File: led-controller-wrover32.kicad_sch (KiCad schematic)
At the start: 54 parts, among them J101 Molex PicoBlade 4-pin, J102 Molex PicoBlade 6-pin, J103 STATUS OUT, J104 USB_B_Micro, J105 POWER IN, J106 Molex PicoBlade 6-pin, J107 5V_LOGIC, Q101 UMH3N, U101 TPS2001DDBVX, U102 USBUF02W6, U103 ESP32-S3-WROOM-2-N32R8, U104 NTS0104BQ,115

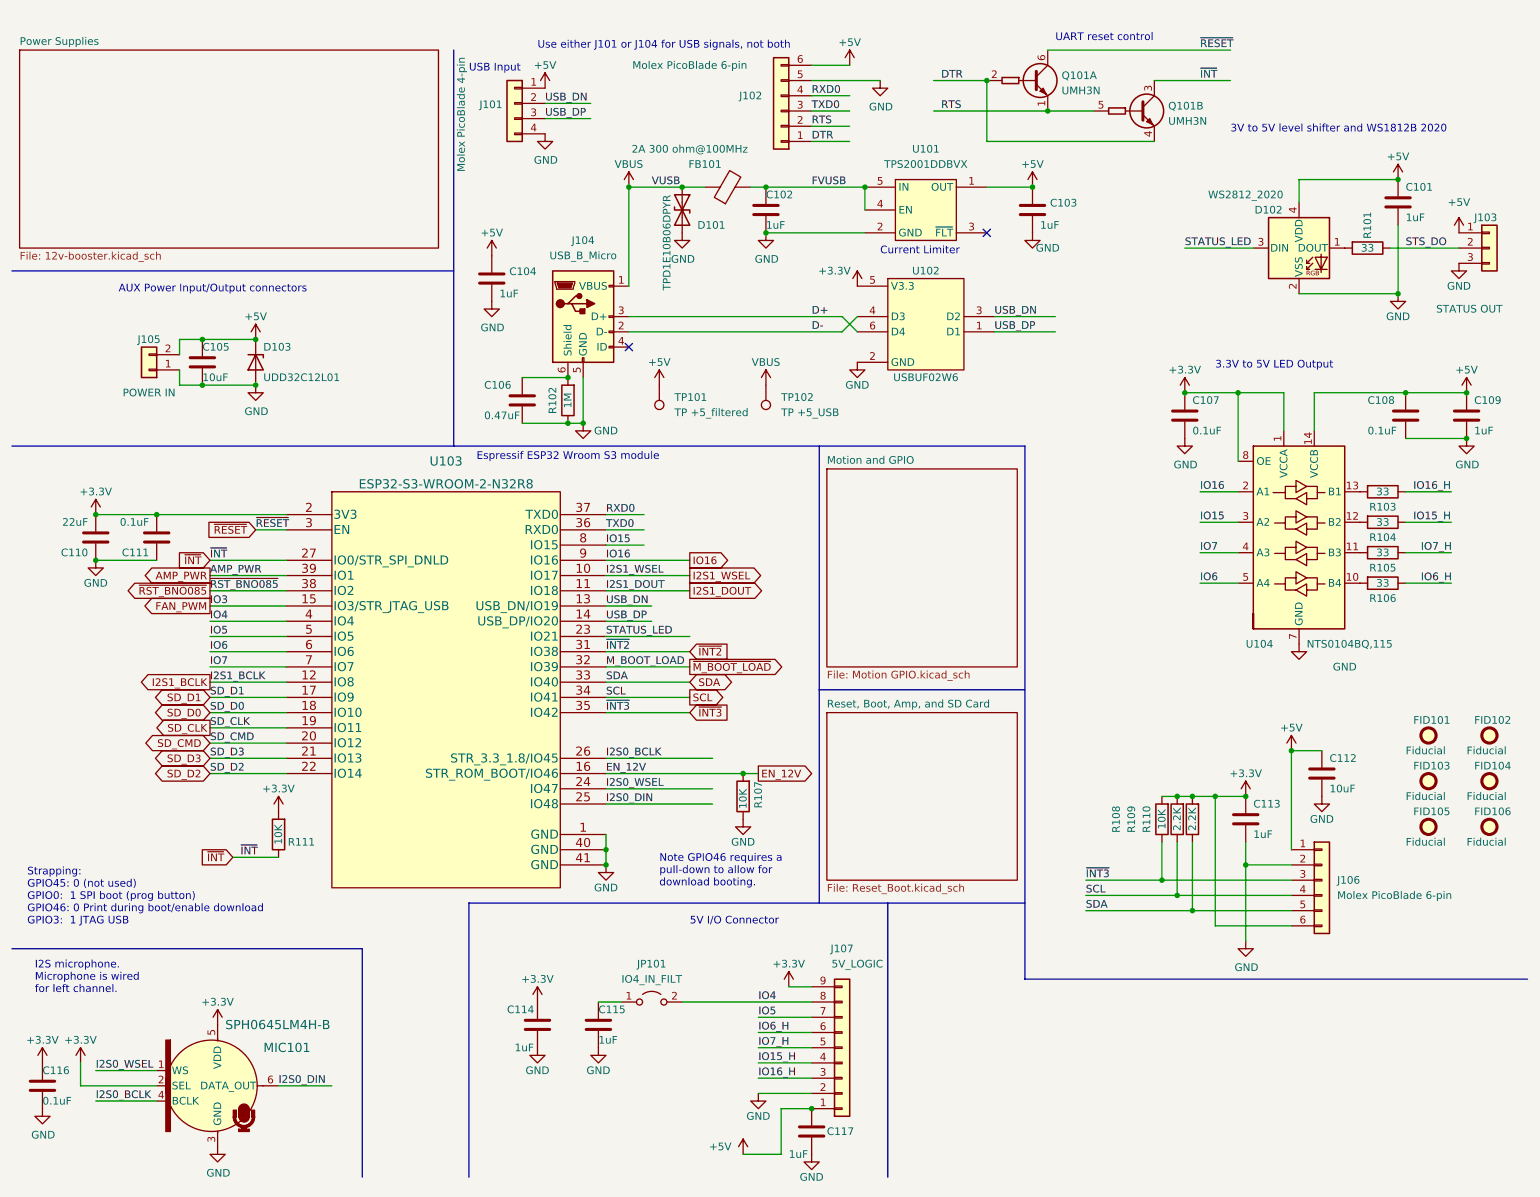
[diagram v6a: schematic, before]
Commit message: Moved to ESP32 S3 Wroom 1
The Wroom 2 requires 1.8V on a couple of GPIOs.  Since I don't need 32MB of
flash the Wroom 1 is used instead.  The footprint is slightly different,
however.

Signed-off-by: Aaron Williams <aaron.w2@gmail.com>
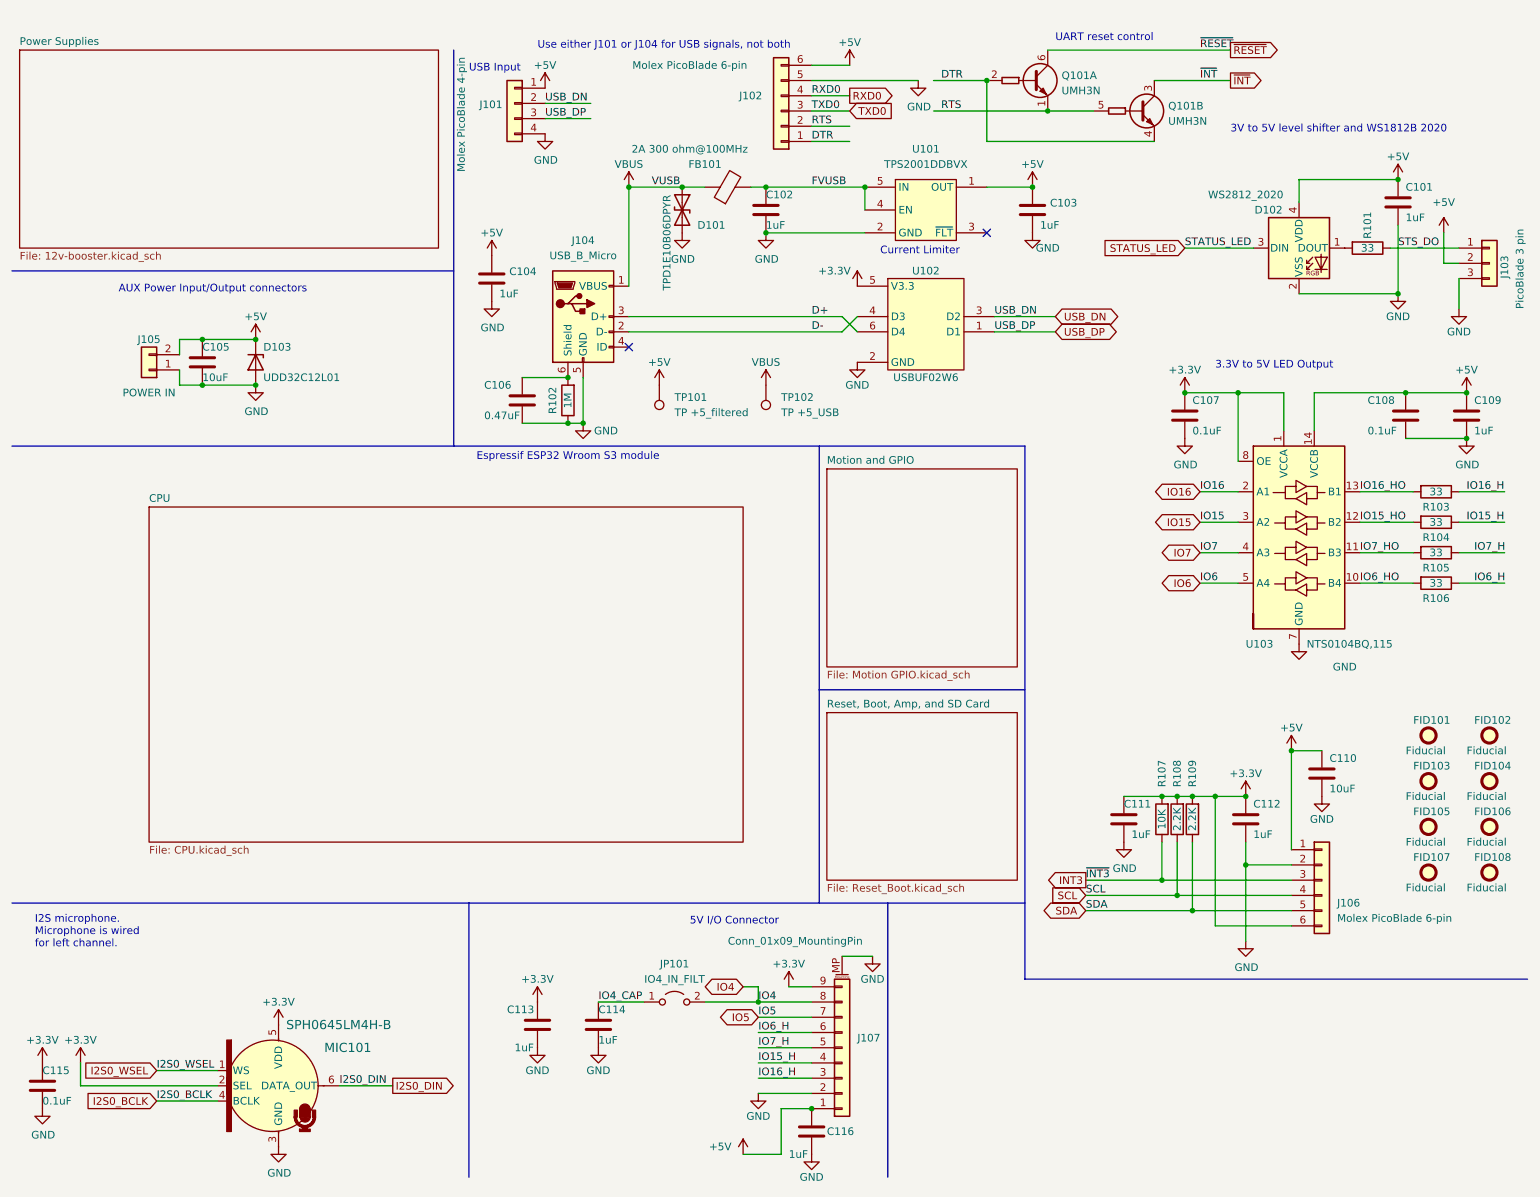
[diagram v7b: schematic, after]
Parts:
- removed C110: 22uF, Capacitor_SMD:C_0603_1608Metric, symbol Device:C
- removed J107: 5V_LOGIC, Connector_JST:JST_SH_BM09B-SRSS-TB_1x09-1MP_P1.00mm_Vertical, symbol Connector_Generic:Conn_01x09
- removed R107, R111: 10K, Resistor_SMD:R_0402_1005Metric, symbol Device:R
- removed U103: ESP32-S3-WROOM-2-N32R8, Espressif:ESP32-S3-WROOM-2, symbol Aaron:ESP32-S3-WROOM-2-N32R8V
- added FID107, FID108: Fiducial, Fiducial:Fiducial_0.5mm_Mask1mm, symbol Mechanical:Fiducial
- added J107: Conn_01x09_MountingPin, Connector_JST:JST_SH_BM09B-SRSS-TB_1x09-1MP_P1.00mm_Vertical, symbol Connector_Generic_MountingPin:Conn_01x09_MountingPin
- C111: value 0.1uF -> 1uF; DESC (none) -> CAP CER 1UF 25V X5R 0402; Digi-Key_PN (none) -> 490-GRM155R61E105MA12JCT-ND; MANUFACTURER (none) -> Murata Electronics; MFR (none) -> Murata Electronics; MPN (none) -> GRM155R61E105MA12J; Manufacturer (none) -> Murata Electronics; Manufacturer Part Number (none) -> GRM155R61E105MA12J; SPN (none) -> 490-GRM155R61E105MA12JCT-ND; SPURL (none) -> https://www.digikey.com/en/products/detail/murata-electroni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
- D103: MFR (none) -> YAGEO; MPN (none) -> UDD32C12L01; Manufacturer Part Number (none) -> UDD32C12L01; SPN (none) -> YAG6692CT-ND; SPR (none) -> Digikey; SPURL (none) -> https://www.digikey.com/en/products/detail/yageo/UDD32C12L0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
- J103: value STATUS OUT -> PicoBlade 3 pin; footprint Connector_JST:JST_SH_BM03B-SRSS-TB_1x03-1MP_P1.00mm_Vertical -> Connector_Molex:Molex_PicoBlade_53047-0310_1x03_P1.25mm_Vertical; MFR JST Sales America Inc. -> Molex; MPN BM03B-SRSS-TBT(LF)(SN) -> 0530470360; SPN 455-2957-1-ND -> 0530470360; SPURL https://www.digikey.com/en/products/detail/jst-sales-americ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 -> https://www.digikey.com/en/products/detail/molex/0530470360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
- renumbered C112 to C110, C113 to C112, C114 to C113, C115 to C114, C116 to C115, C117 to C116, R108 to R107, R109 to R108, R110 to R109, U104 to U103
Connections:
- net +3V3: now also J107.9 (Pin_9)
- net +5V: now also J103.2 (Pin_2), J107.1 (Pin_1); no longer J103.1 (Pin_1)
- net GND: now also J103.1 (Pin_1), R101.1, J107.2 (Pin_2), J107.MP (MountPin)
- net IO15_H: now also J107.4 (Pin_4)
- net IO16_H: now also J107.3 (Pin_3)
- net IO4: now also J107.8 (Pin_8)
- net IO5: now also J107.7 (Pin_7)
- net IO6_H: now also J107.6 (Pin_6)
- net IO7_H: now also J107.5 (Pin_5)
- net IO16_HO: now reaches R103.2, U103.13 (B1)
- net IO4_CAP: now reaches C114.1, JP101.1 (A)
- net IO6_HO: now reaches R106.2, U103.10 (B4)
- net IO7_HO: now reaches R105.2, U103.11 (B3)
- net IO15_HO: now reaches R104.2, U103.12 (B2)
- removed net STS_DO: J103.2 (Pin_2), R101.1
- net ~{INT3} renamed INT3
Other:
- added sheet CPU (CPU.kicad_sch)
- note removed: "Note GPIO46 requires a pull-down to allow for download booting."
- note removed: "Strapping: GPIO45: 0 (not used) GPIO0: 1 SPI boot (prog button) GPIO46: 0 Print during boot/enable download GPIO3: 1 JTAG USB"
- moved on the sheet: JP101, MIC101, R103, R104, R105, R106

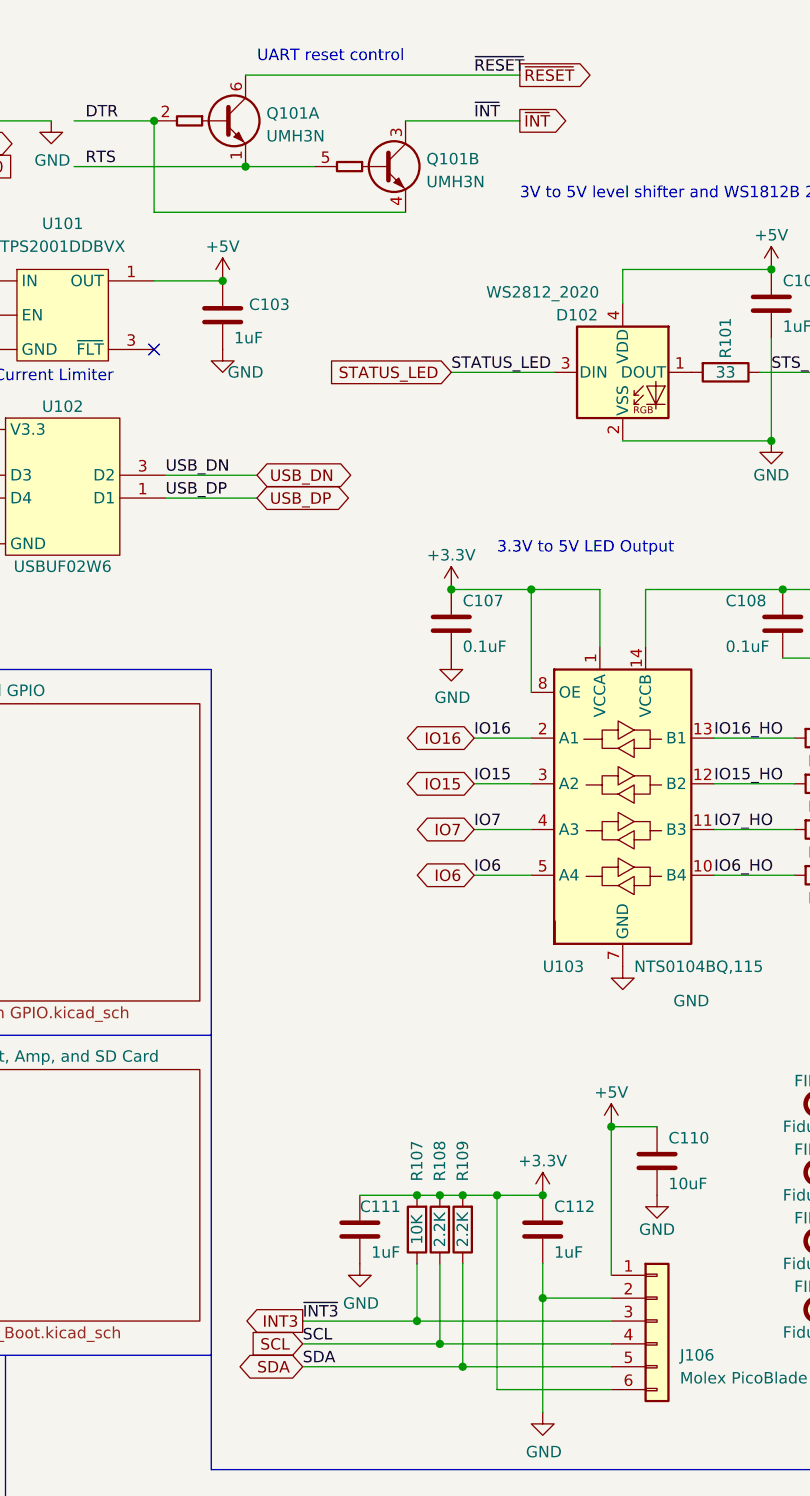
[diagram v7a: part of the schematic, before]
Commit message: Changed ESP32 to ESP32-S3-WROOM-1 and other cleanup
Signed-off-by: Aaron Williams <aaron.w2@gmail.com>
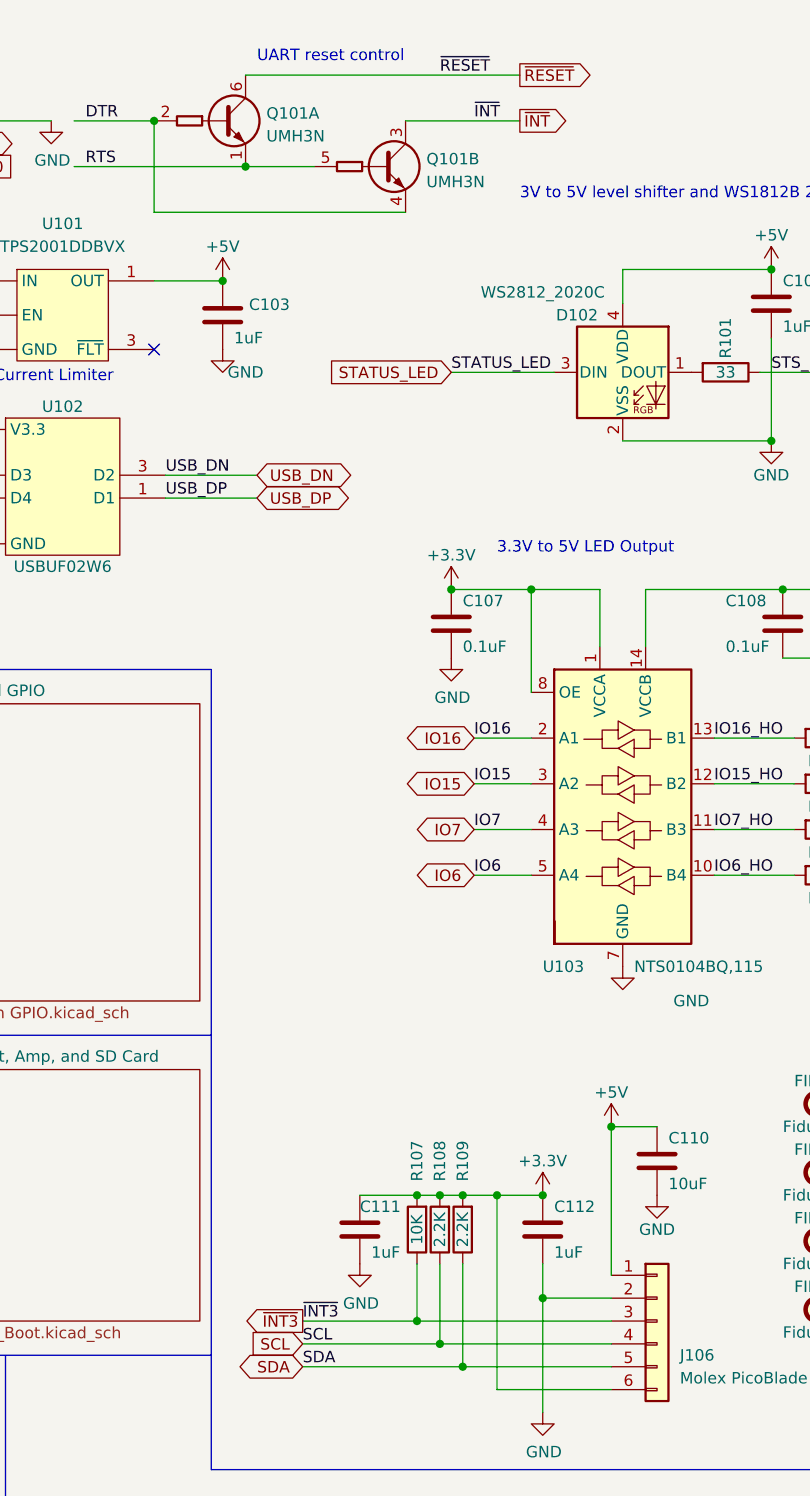
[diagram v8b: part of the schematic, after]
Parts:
- D102: value WS2812_2020 -> WS2812_2020C; MPN (none) -> WS2812C-2020; SPN (none) -> C2976072; SPR (none) -> lcsc; SPURL (none) -> https://www.lcsc.com/product-detail/Light-Emitting-Diodes-L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
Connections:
- net INT3 renamed ~{INT3}
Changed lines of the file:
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@@
   (title_block
     (title "Wroom32 LED Controller")
-    (date "2022-12-02")
+    (date "2022-12-06")
     (rev "4.0.0")
     (company "Aaron Williams")
@@
     (effects (font (size 1.27 1.27)) (justify left bottom))
   )
-  (label "~{RESET}" (at 210.82 15.24 0)
+  (label "~{RESET}" (at 207.01 15.24 0)
     (effects (font (size 1.27 1.27)) (justify left bottom))
   )
@@
     )
   )
-  (global_label "INT3" (shape output) (at 191.77 153.67 180) (fields_autoplaced)
+  (global_label "~{INT3}" (shape output) (at 191.77 153.67 180) (fields_autoplaced)
     (effects (font (size 1.27 1.27)) (justify right))
     (property "Intersheet References" "${INTERSHEET_REFS}" (id 0) (at 185.3334 153.5906 0)
@@
     (in_bom yes) (on_board yes)
     (property "Reference" "D102" (id 0) (at 222.25 41.91 0))
-    (property "Value" "WS2812_2020" (id 1) (at 218.44 39.37 0))
+    (property "Value" "WS2812_2020C" (id 1) (at 218.44 39.37 0))
     (property "Footprint" "Aaron:LED_WS2812_2020" (id 2) (at 228.6 55.88 0)
       (effects (font (size 1.27 1.27)) (justify left top) hide)
@@
       (effects (font (size 1.27 1.27)) hide)
     )
+    (property "MPN" "WS2812C-2020" (id 5) (at 227.33 48.26 0)
+      (effects (font (size 1.27 1.27)) hide)
+    )
+    (property "SPR" "lcsc" (id 6) (at 227.33 48.26 0)
+      (effects (font (size 1.27 1.27)) hide)
+    )
+    (property "SPN" "C2976072" (id 7) (at 227.33 48.26 0)
+      (effects (font (size 1.27 1.27)) hide)
+    )
+    (property "SPURL" "https://www.lcsc.com/product-detail/Light-Emitting-Diodes-LED_Worldsemi-WS2812C-2020-V1_C2976072.html" (id 8) (at 227.33 48.26 0)
+      (effects (font (size 1.27 1.27)) hide)
+    )
     (pin "1")
     (pin "2")
@@
     )
     (path "/37728e43-6383-443b-bd09-8141c8a031c2"
-      (reference "D102") (unit 1) (value "WS2812_2020") (footprint "Aaron:LED_WS2812_2020")
+      (reference "D102") (unit 1) (value "WS2812_2020C") (footprint "Aaron:LED_WS2812_2020")
     )
     (path "/ab86f464-febf-4958-8f04-64499b1eee62"
